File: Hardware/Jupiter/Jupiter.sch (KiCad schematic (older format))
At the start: 92 parts

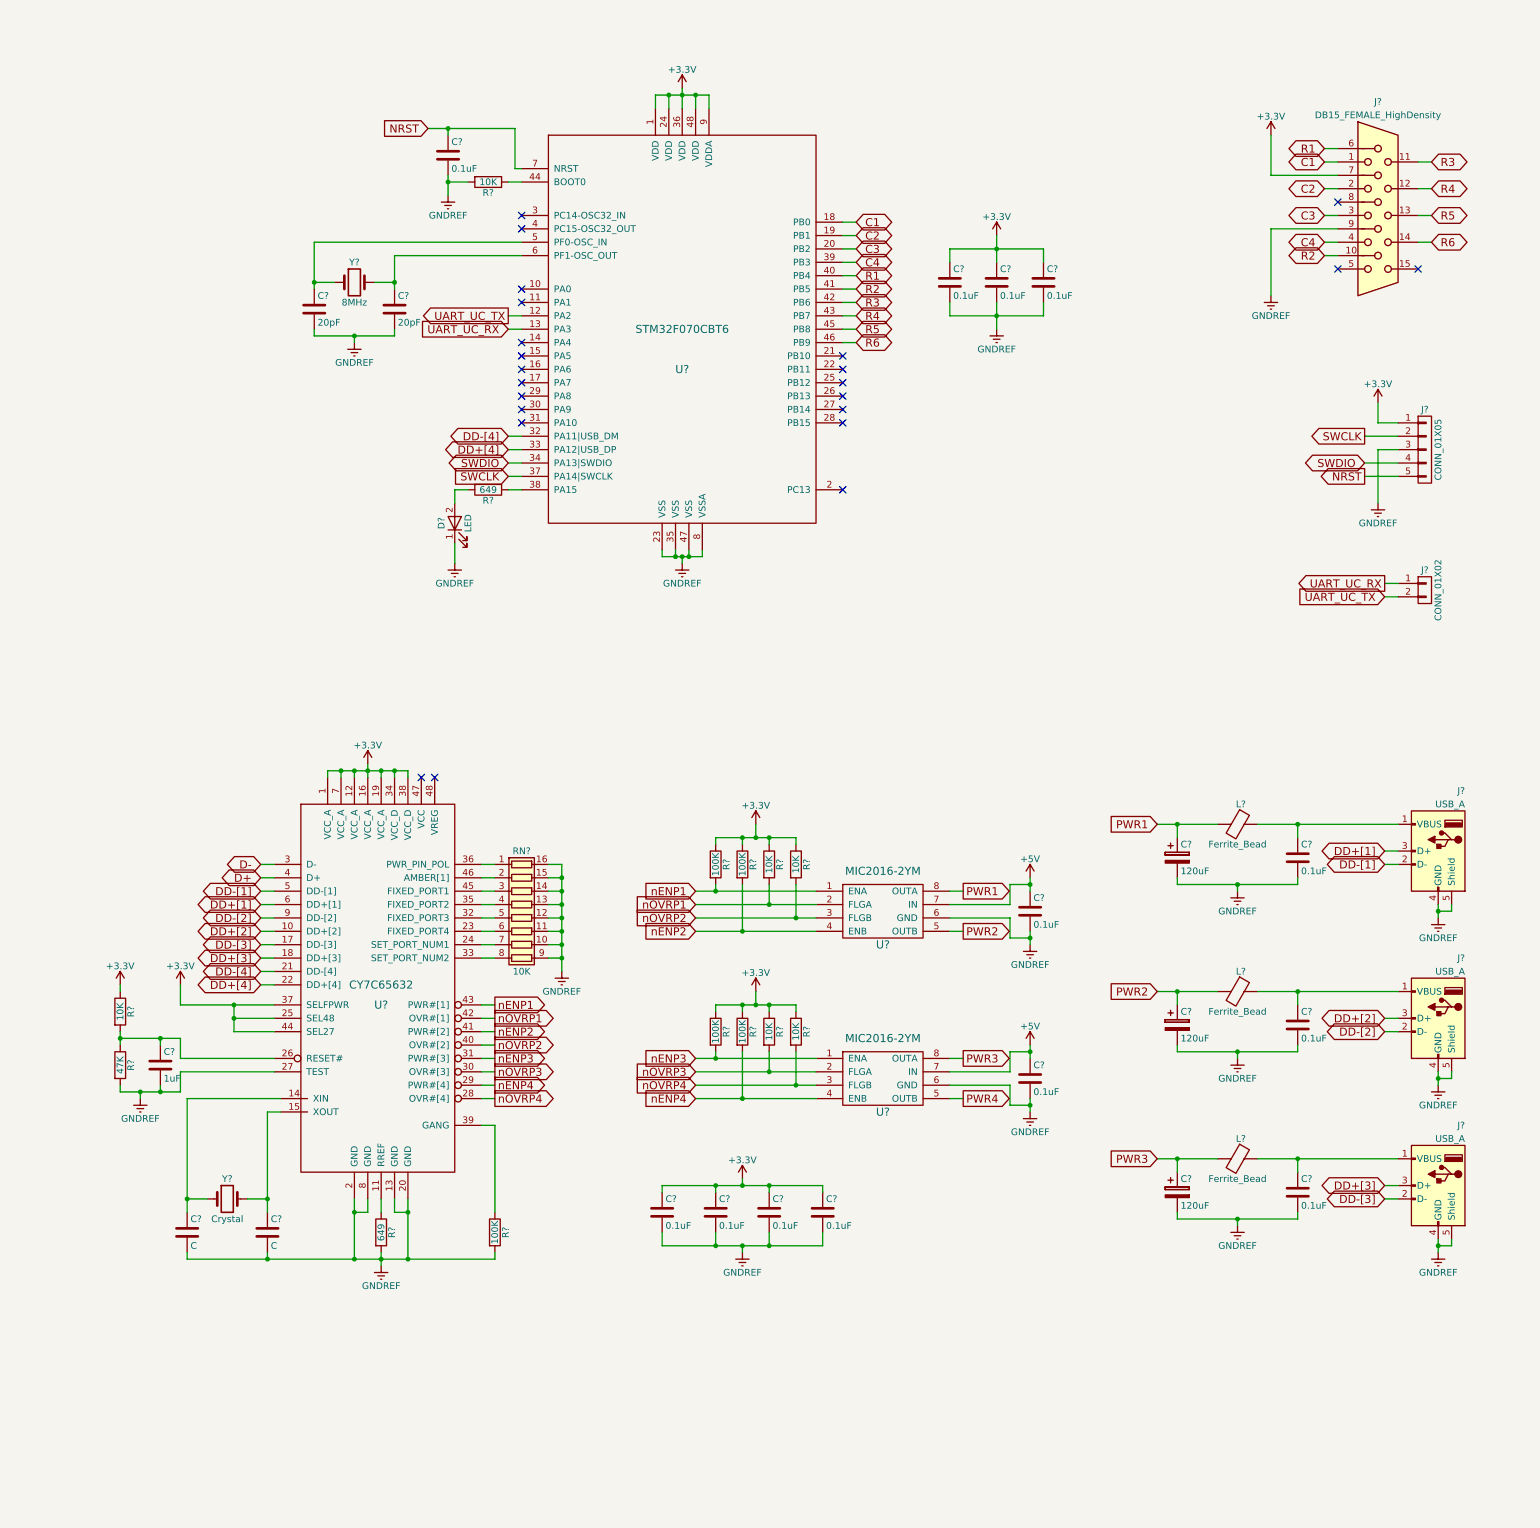
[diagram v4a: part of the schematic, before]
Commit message: Add a DB9 port to allow for using Sega Mega Drive controllers as well.
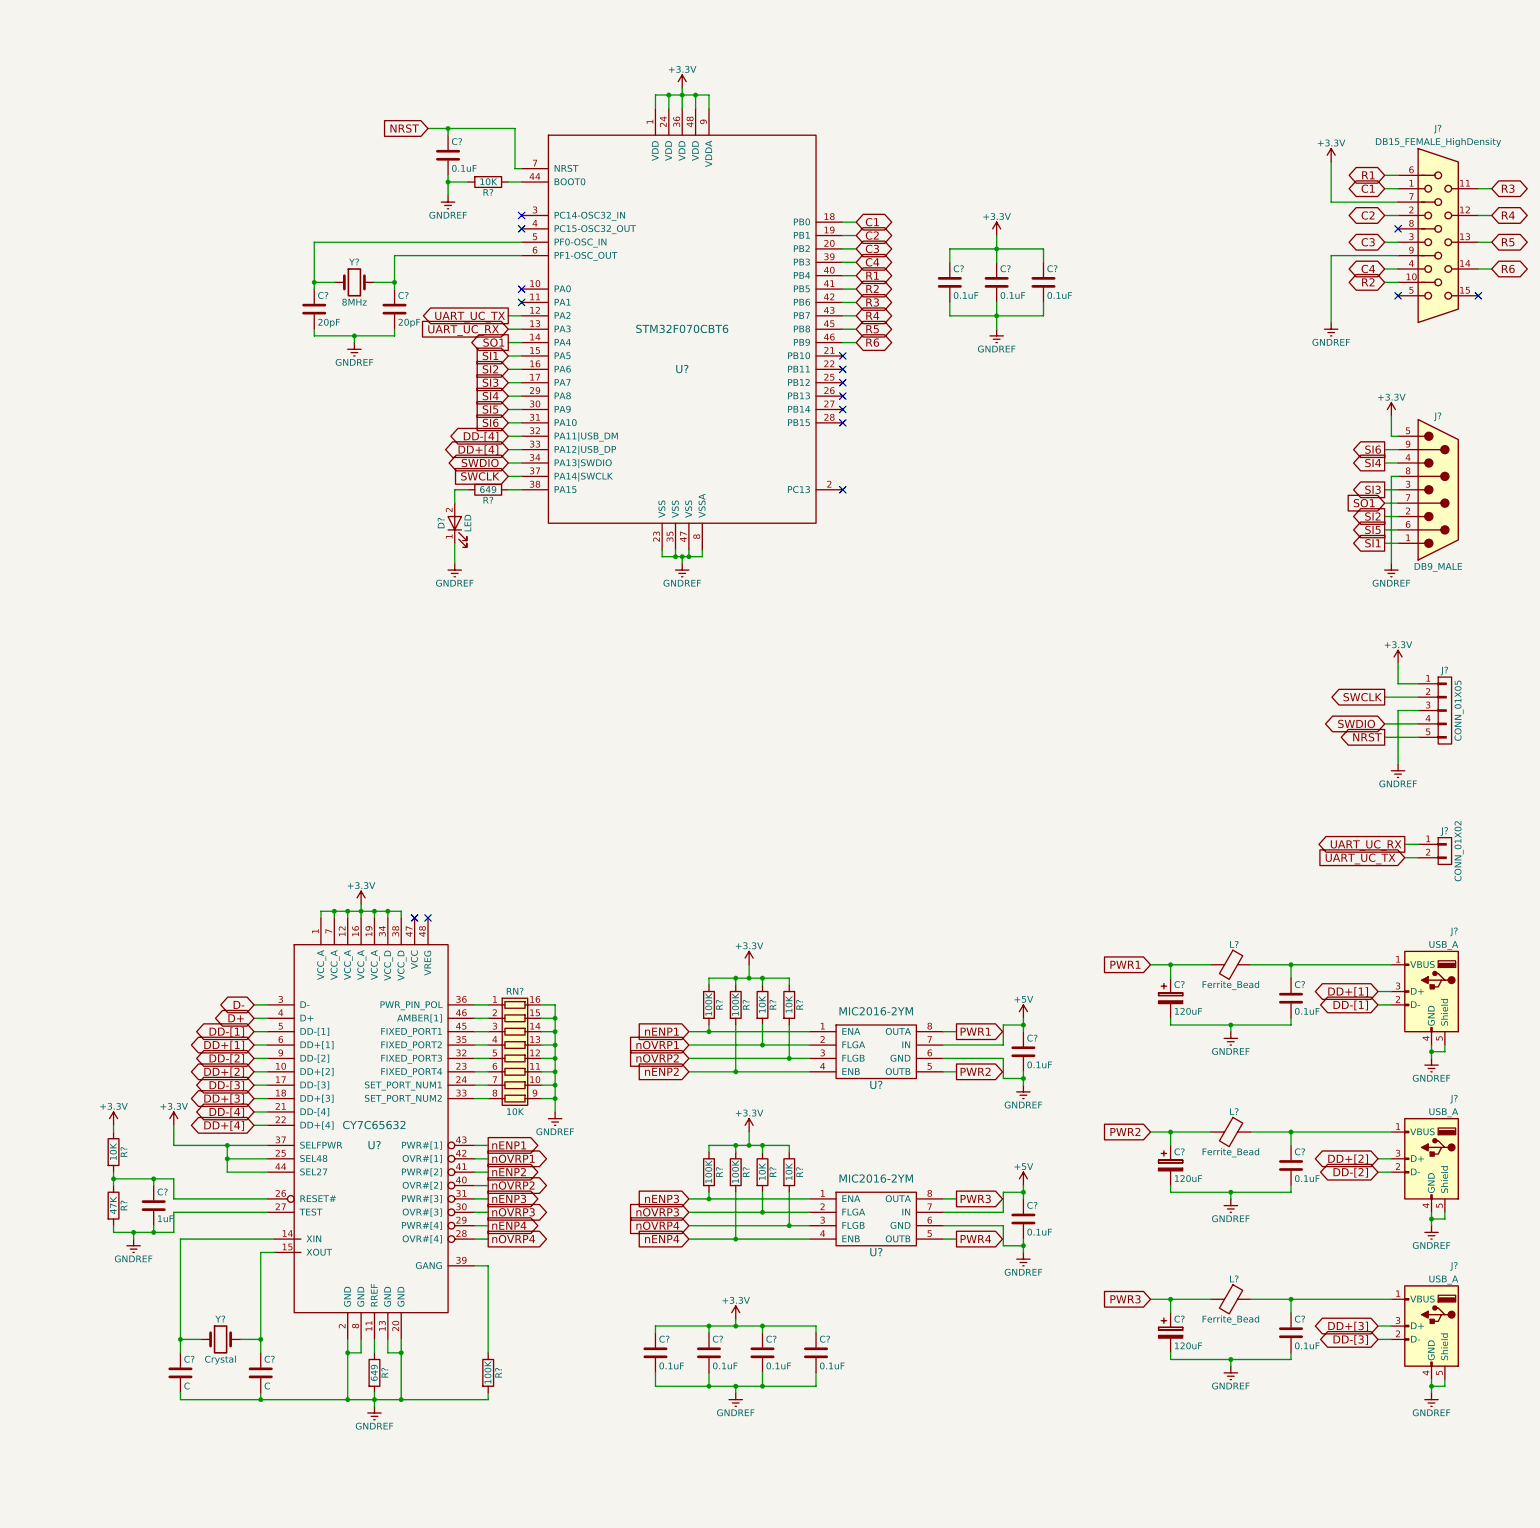
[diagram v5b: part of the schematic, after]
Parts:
- added J?: DB9_MALE, symbol DB9_MALE
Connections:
- net +3V3: now also J?.5
- net GNDREF: now also J?.8
- net SO1: now reaches U?.14 (PA4)
- net SO1: now also J?.7
- net SI1: now reaches U?.15 (PA5)
- net SI1: now also J?.1
- net SI2: now reaches U?.16 (PA6)
- net SI2: now also J?.2
- net SI3: now reaches U?.17 (PA7)
- net SI3: now also J?.3
- net SI4: now reaches U?.29 (PA8)
- net SI4: now also J?.4
- net SI5: now reaches U?.30 (PA9)
- net SI5: now also J?.6
- net SI6: now reaches U?.31 (PA10)
- net SI6: now also J?.9
- no-connect marks 26 -> 19
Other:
- moved on the sheet: C?, J?, L?, R?, RN?, U?, Y?
